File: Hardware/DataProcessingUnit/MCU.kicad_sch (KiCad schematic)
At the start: 43 parts, among them J1 USB_B_Micro, J4 Conn_01x07, Q2 BC847, SW1 SW_Push, U3 STM32F103RBTx, Y1 32,768kHz, Y2 Crystal

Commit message: corections after hw sw integration
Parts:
- C11, C12: value 6p8 -> 10p
- C13, C14: value 6p8 -> 22p
- C9: value 100n -> 1u
- R13, R14: value TBD -> 0R
- R18: value 36k -> 39k
- Y1: value 32,768kHz -> 32,768kHz /12.5p
- Y2: value Crystal -> 8M
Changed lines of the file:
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@@
 			)
 		)
-		(property "Value" "Crystal"
+		(property "Value" "8M"
 			(at 87.63 147.3199 90)
 			(effects
@@
 			)
 		)
-		(property "Value" "6p8"
+		(property "Value" "10p"
 			(at 78.74 116.84 90)
 			(effects
@@
 			)
 		)
-		(property "Value" "32,768kHz"
+		(property "Value" "32,768kHz /12.5p"
 			(at 87.63 111.7599 90)
 			(effects
@@
 			)
 		)
-		(property "Value" "6p8"
+		(property "Value" "10p"
 			(at 78.74 97.79 90)
 			(effects
@@
 			)
 		)
-		(property "Value" "6p8"
+		(property "Value" "22p"
 			(at 78.74 152.4 90)
 			(effects
@@
 			)
 		)
-		(property "Value" "TBD"
+		(property "Value" "0R"
 			(at 88.9 134.62 90)
 			(effects
@@
 			)
 		)
-		(property "Value" "36k"
+		(property "Value" "39k"
 			(at 48.26 44.4499 0)
 			(effects
@@
 			)
 		)
-		(property "Value" "100n"
+		(property "Value" "1u"
 			(at 35.56 120.6499 0)
 			(effects
@@
 			)
 		)
-		(property "Value" "6p8"
+		(property "Value" "22p"
 			(at 78.74 133.35 90)
 			(effects
@@
 			)
 		)
-		(property "Value" "TBD"
+		(property "Value" "0R"
 			(at 88.9 153.67 90)
 			(effects

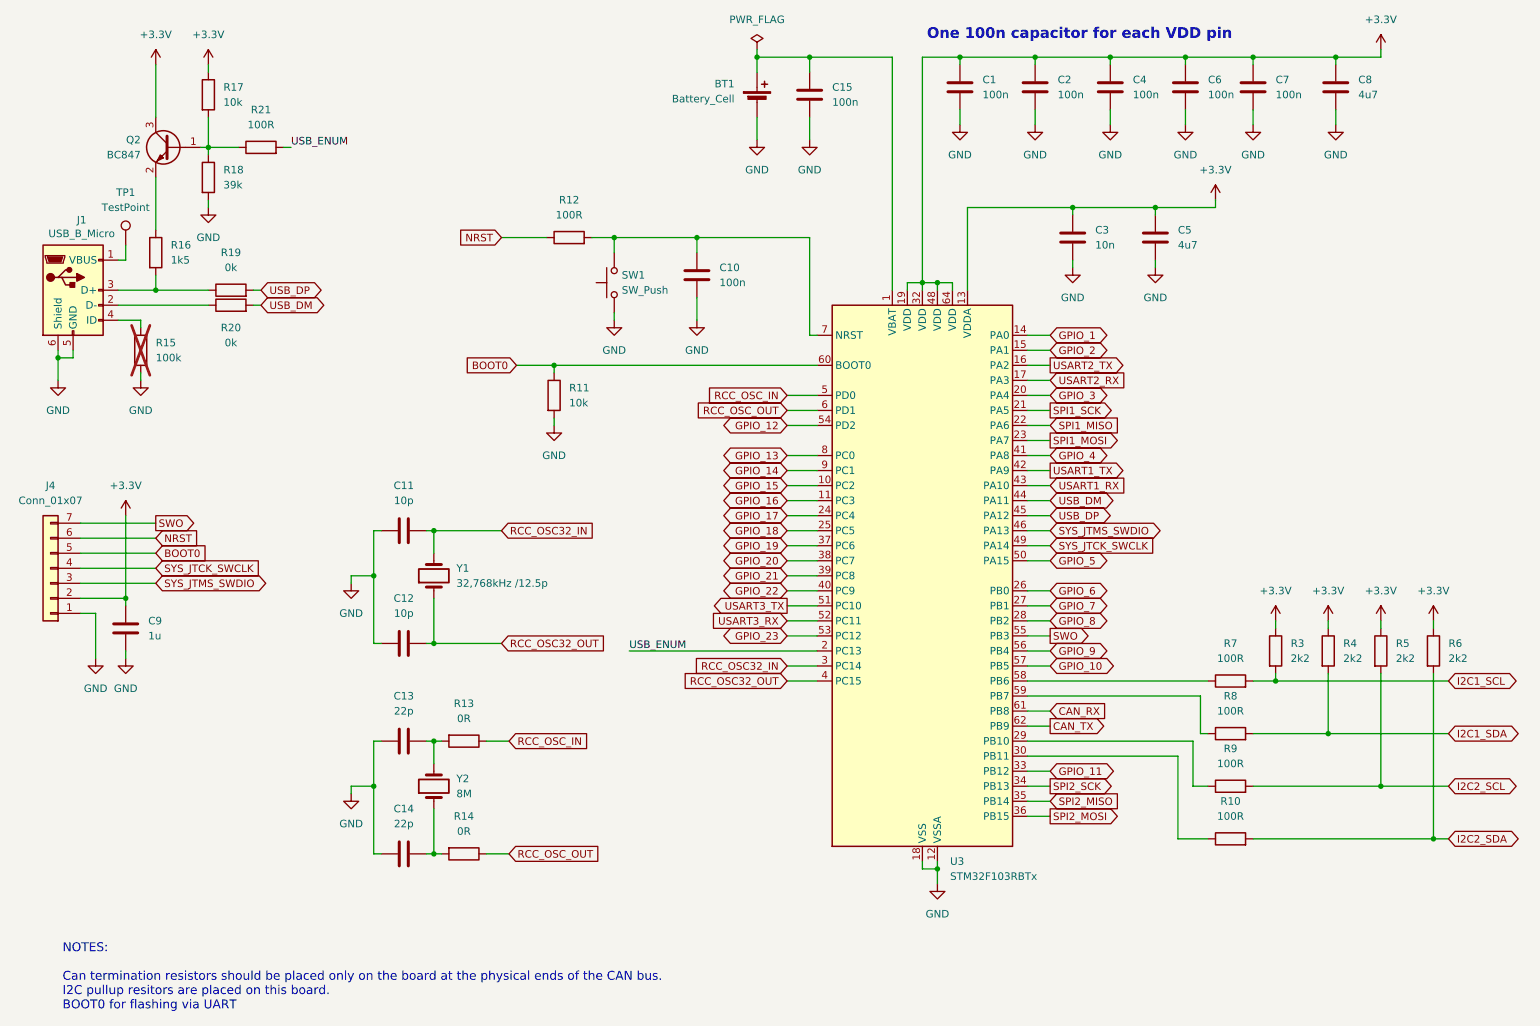
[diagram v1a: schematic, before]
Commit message: rework CI, make PCB smaller
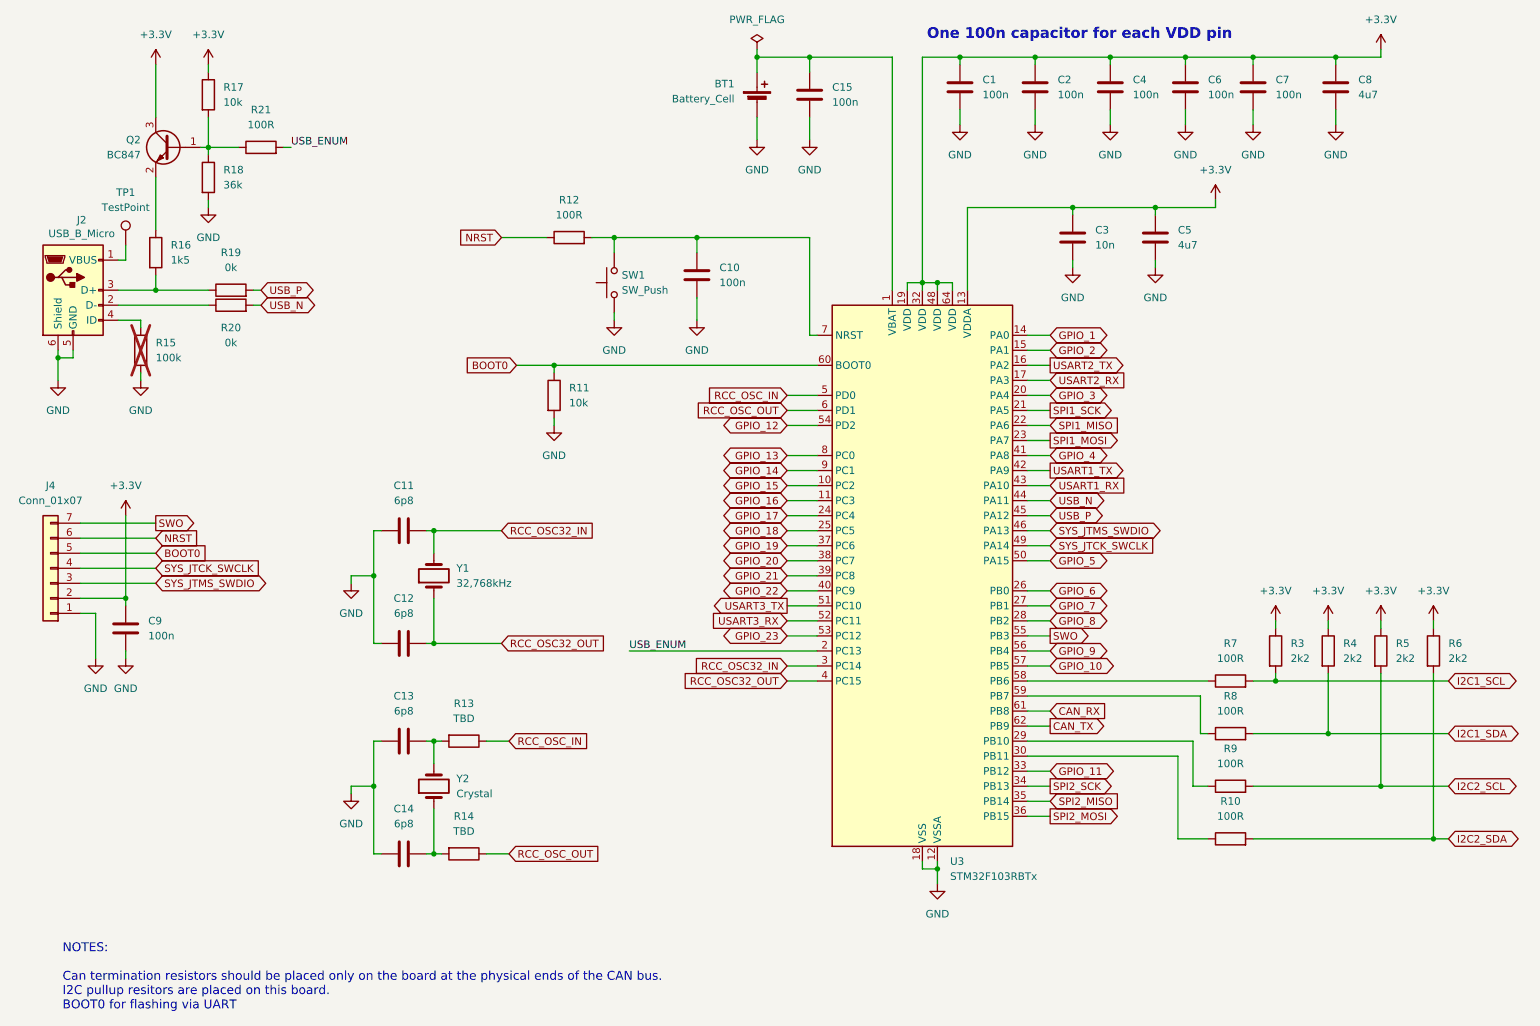
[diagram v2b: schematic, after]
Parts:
- removed J1: USB_B_Micro, Connector_USB:USB_Micro-B_Molex-105017-0001, symbol Connector:USB_B_Micro
- added J2: USB_B_Micro, HardwareDataLogger:USB_Micro-B_Molex-105017-0001_Extra_Mechanical_Pads, symbol Connector:USB_B_Micro
- C11, C12: value 10p -> 6p8
- C13, C14: value 22p -> 6p8
- C9: value 1u -> 100n
- R13, R14: value 0R -> TBD
- R18: value 39k -> 36k
- Y1: value 32,768kHz /12.5p -> 32,768kHz
- Y2: value 8M -> Crystal
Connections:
- net GND: now also J2.5 (GND), J2.6 (Shield)
- net at R20.1: now also J2.2 (D-)
- net at TP1.1: now also J2.1 (VBUS)
- net at R16.2, R19.1: now also J2.3 (D+)
- net at R15.1: now also J2.4 (ID)
- net USB_DM renamed USB_N
- net USB_DP renamed USB_P
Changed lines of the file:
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@@
 		)
 	)
-	(global_label "USB_DM"
+	(global_label "USB_N"
 		(shape bidirectional)
 		(at 187.96 97.79 0)
@@
 		)
 		(property "Intersheetrefs" "${INTERSHEET_REFS}"
-			(at 199.5555 97.79 0)
+			(at 198.1646 97.79 0)
 			(effects
 				(font
@@
 		)
 	)
-	(global_label "USB_DP"
+	(global_label "USB_P"
 		(shape bidirectional)
 		(at 54.61 62.23 0)
@@
 		)
 		(property "Intersheetrefs" "${INTERSHEET_REFS}"
-			(at 66.0241 62.23 0)
+			(at 64.7541 62.23 0)
 			(effects
 				(font
@@
 		)
 	)
-	(global_label "USB_DM"
+	(global_label "USB_N"
 		(shape bidirectional)
 		(at 54.61 64.77 0)
@@
 		)
 		(property "Intersheetrefs" "${INTERSHEET_REFS}"
-			(at 66.2055 64.77 0)
+			(at 64.8146 64.77 0)
 			(effects
 				(font
@@
 		)
 	)
-	(global_label "USB_DP"
+	(global_label "USB_P"
 		(shape bidirectional)
 		(at 187.96 100.33 0)
@@
 		)
 		(property "Intersheetrefs" "${INTERSHEET_REFS}"
-			(at 199.3741 100.33 0)
+			(at 198.1041 100.33 0)
 			(effects
 				(font
@@
 			)
 		)
-		(property "Value" "8M"
+		(property "Value" "Crystal"
 			(at 87.63 147.3199 90)
 			(effects
@@
 			)
 		)
-		(property "Value" "10p"
+		(property "Value" "6p8"
 			(at 78.74 116.84 90)
 			(effects
@@
 			)
 		)
-		(property "Value" "32,768kHz /12.5p"
+		(property "Value" "32,768kHz"
 			(at 87.63 111.7599 90)
 			(effects
@@
 			)
 		)
-		(property "Value" "10p"
+		(property "Value" "6p8"
 			(at 78.74 97.79 90)
 			(effects
@@
 			)
 		)
-		(property "Value" "22p"
+		(property "Value" "6p8"
 			(at 78.74 152.4 90)
 			(effects
@@
 	)
 	(symbol
-		(lib_id "Connector:USB_B_Micro")
-		(at 22.86 62.23 0)
-		(unit 1)
-		(exclude_from_sim no)
-		(in_bom yes)
-		(on_board yes)
-		(dnp no)
-		(property "Reference" "J1"
-			(at 24.3078 50.3682 0)
-			(effects
-				(font
-					(size 1.27 1.27)
-				)
-			)
-		)
-		(property "Value" "USB_B_Micro"
-			(at 24.3078 52.6796 0)
-			(effects
-				(font
-					(size 1.27 1.27)
-				)
-			)
-		)
-		(property "Footprint" "Connector_USB:USB_Micro-B_Molex-105017-0001"
-			(at 26.67 63.5 0)
-			(effects
-				(font
-					(size 1.27 1.27)
-				)
-				(hide yes)
-			)
-		)
-		(property "Datasheet" "~"
-			(at 26.67 63.5 0)
-			(effects
-				(font
-					(size 1.27 1.27)
-				)
-				(hide yes)
-			)
-		)
-		(property "Description" ""
-			(at 22.86 62.23 0)
-			(effects
-				(font
-					(size 1.27 1.27)
-				)
-				(hide yes)
-			)
-		)
-		(pin "1"
-		)
-		(pin "2"
-		)
-		(pin "3"
-		)
-		(pin "4"
-		)
-		(pin "5"
-		)
-		(pin "6"
-		)
-		(instances
-			(project "DataProcessingUnit"
-				(path "/18f4643d-59cf-40d8-90af-99b4dbe1f32f/9bdfab82-cef8-460c-a16e-388f6d900e76"
-					(reference "J1")
-					(unit 1)
-				)
-			)
-		)
-	)
-	(symbol
 		(lib_id "Device:C")
 		(at 222.25 27.94 0)
@@
 			)
 		)
-		(property "Value" "0R"
+		(property "Value" "TBD"
 			(at 88.9 134.62 90)
 			(effects
@@
 	)
 	(symbol
+		(lib_id "Connector:USB_B_Micro")
+		(at 22.86 62.23 0)
+		(unit 1)
+		(exclude_from_sim no)
+		(in_bom yes)
+		(on_board yes)
+		(dnp no)
+		(property "Reference" "J2"
+			(at 24.3078 50.3682 0)
+			(effects
+				(font
+					(size 1.27 1.27)
+				)
+			)
+		)
+		(property "Value" "USB_B_Micro"
+			(at 24.3078 52.6796 0)
+			(effects
+				(font
+					(size 1.27 1.27)
+				)
+			)
+		)
+		(property "Footprint" "HardwareDataLogger:USB_Micro-B_Molex-105017-0001_Extra_Mechanical_Pads"
+			(at 26.67 63.5 0)
+			(effects
+				(font
+					(size 1.27 1.27)
+				)
+				(hide yes)
+			)
+		)
+		(property "Datasheet" "~"
+			(at 26.67 63.5 0)
+			(effects
+				(font
+					(size 1.27 1.27)
+				)
+				(hide yes)
+			)
+		)
+		(property "Description" "USB Micro Type B connector"
+			(at 22.86 62.23 0)
+			(effects
+				(font
+					(size 1.27 1.27)
+				)
+				(hide yes)
+			)
+		)
+		(pin "1"
+		)
+		(pin "2"
+		)
+		(pin "3"
+		)
+		(pin "4"
+		)
+		(pin "5"
+		)
+		(pin "6"
+		)
+		(instances
+			(project "DataProcessingUnit"
+				(path "/18f4643d-59cf-40d8-90af-99b4dbe1f32f/9bdfab82-cef8-460c-a16e-388f6d900e76"
+					(reference "J2")
+					(unit 1)
+				)
+			)
+		)
+	)
+	(symbol
 		(lib_id "power:+3.3V")
 		(at 234.95 118.11 0)
@@
 			)
 		)
-		(property "Value" "39k"
+		(property "Value" "36k"
 			(at 48.26 44.4499 0)
 			(effects
@@
 			)
 		)
-		(property "Value" "1u"
+		(property "Value" "100n"
 			(at 35.56 120.6499 0)
 			(effects
@@
 			)
 		)
-		(property "Value" "22p"
+		(property "Value" "6p8"
 			(at 78.74 133.35 90)
 			(effects
@@
 			)
 		)
-		(property "Value" "0R"
+		(property "Value" "TBD"
 			(at 88.9 153.67 90)
 			(effects
